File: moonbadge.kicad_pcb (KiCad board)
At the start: 2 copper layers, 49.5 x 147.2 mm, 61 parts, among them J1 Conn_01x04, J10 105162-0001, J2 USB_B_Micro, J3 Conn_01x02, J4 Conn_01x02, J5 Conn_01x02, J6 Conn_01x04, J7 Conn_01x02, J8 Conn_01x02, J9 Conn_01x02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

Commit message: split boards into top and bottom
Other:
- outline, holes or cut-outs redrawn

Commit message: removed designators, more cosmetic fixes
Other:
- board text added: "MoonBadge.github.io"
- board text added: "Moonbadge Rev.1 Alex Camilo"

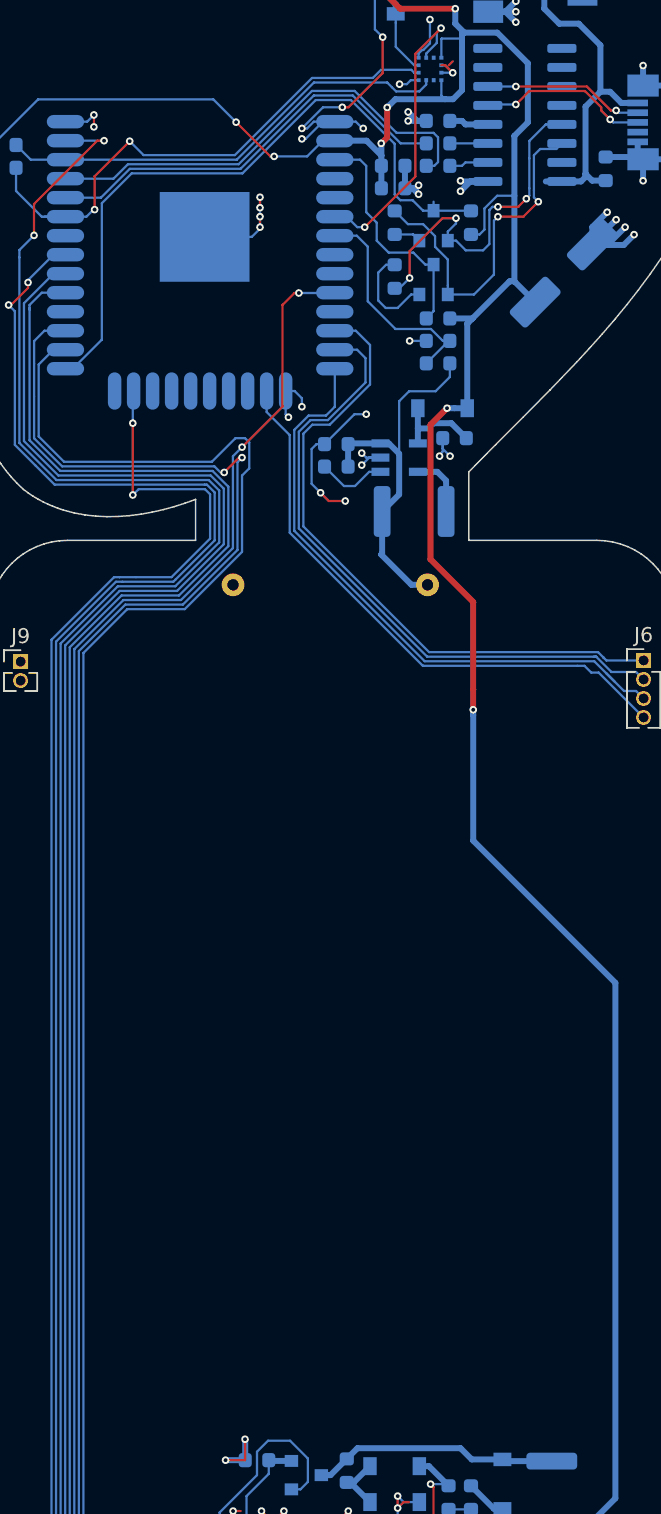
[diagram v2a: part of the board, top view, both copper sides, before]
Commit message: Rev 2
Swapped TX/RX
Swapped battery polarity
nudged battery down by 1mm to clear boost coil
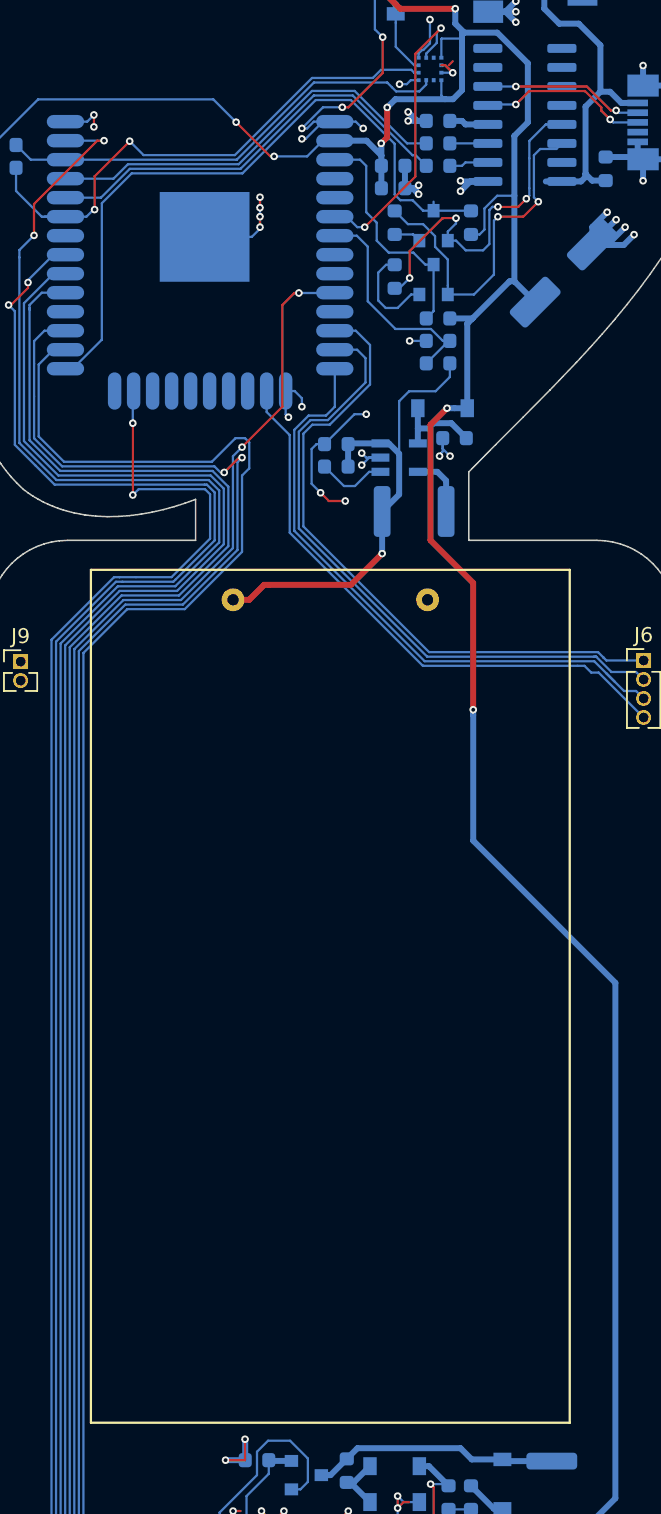
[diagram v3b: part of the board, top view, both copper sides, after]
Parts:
- BT1: moved to F.Cu
- moved BT1 1.00 mm to (139.9, 81.7)
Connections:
- R11 pad 1: RxD -> TxD
- R8 pad 1: TxD -> RxD
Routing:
- net BAT: track 24.9 -> 32.2 mm, vias 0 -> 1
- net TxD: track 31.2 -> 28.0 mm
- net RxD: track 28.3 -> 28.9 mm
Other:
- board text added: "Moonbadge Rev.2 Alex Camilo"
- board text removed: "Moonbadge Rev.1 Alex Camilo"
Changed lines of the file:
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@@
   (page A4)
   (layers
-    (0 F.Cu signal)
+    (0 F.Cu signal hide)
     (31 B.Cu signal)
     (32 B.Adhes user)
@@
     (35 F.Paste user)
     (36 B.SilkS user)
-    (37 F.SilkS user hide)
+    (37 F.SilkS user)
     (38 B.Mask user)
     (39 F.Mask user)
@@
     (visible_elements 7FFFFFFF)
     (pcbplotparams
-      (layerselection 0x010fc_ffffffff)
+      (layerselection 0x010f0_7ffffffe)
       (usegerberextensions false)
       (usegerberattributes false)
@@
       (padsonsilk false)
       (subtractmaskfromsilk false)
-      (outputformat 1)
+      (outputformat 5)
       (mirror false)
-      (drillshape 1)
+      (drillshape 0)
       (scaleselection 1)
-      (outputdirectory ""))
+      (outputdirectory "holes"))
   )
   (net 0 "")
@@
     )
   )
-  (module 12BH321P-GR:12BH321P-GR (layer B.Cu)
-    (at 139.9 80.7 90)
-    (fp_text reference BT1 (at -40 17 -90) (layer B.SilkS) hide
-      (effects (font (size 1 1) (thickness 0.15)) (justify mirror))
+  (module 12BH321P-GR:12BH321P-GR (layer F.Cu)
+    (at 139.9 81.7 90)
+    (fp_text reference BT1 (at -40 -17 90) (layer F.SilkS) hide
+      (effects (font (size 1 1) (thickness 0.15)))
     )
-    (fp_text value Battery_Cell (at -49 17 -90) (layer B.Fab)
-      (effects (font (size 1 1) (thickness 0.15)) (justify mirror))
+    (fp_text value Battery_Cell (at -49 -17 90) (layer F.Fab)
+      (effects (font (size 1 1) (thickness 0.15)))
     )
-    (fp_line (start -55 16) (end -55 -16) (layer B.SilkS) (width 0.15))
-    (fp_line (start 2 -16) (end -55 -16) (layer B.SilkS) (width 0.15))
-    (fp_line (start 2 0) (end 2 -16) (layer B.SilkS) (width 0.15))
-    (fp_line (start 2 16) (end 2 0) (layer B.SilkS) (width 0.15))
-    (fp_line (start 2 16) (end -55 16) (layer B.SilkS) (width 0.15))
-    (pad 1 thru_hole circle (at 0 6.5 90) (size 1.524 1.524) (drill 0.762) (layers *.Cu *.Mask)
+    (fp_line (start -55 -16) (end -55 16) (layer F.SilkS) (width 0.15))
+    (fp_line (start 2 16) (end -55 16) (layer F.SilkS) (width 0.15))
+    (fp_line (start 2 0) (end 2 16) (layer F.SilkS) (width 0.15))
+    (fp_line (start 2 -16) (end 2 0) (layer F.SilkS) (width 0.15))
+    (fp_line (start 2 -16) (end -55 -16) (layer F.SilkS) (width 0.15))
+    (pad 1 thru_hole circle (at 0 -6.5 90) (size 1.524 1.524) (drill 0.762) (layers *.Cu *.Mask)
       (net 2 BAT))
-    (pad 2 thru_hole circle (at 0 -6.5 90) (size 1.524 1.524) (drill 0.762) (layers *.Cu *.Mask)
+    (pad 2 thru_hole circle (at 0 6.5 90) (size 1.524 1.524) (drill 0.762) (layers *.Cu *.Mask)
       (net 4 GND))
   )
@@
     )
     (pad 1 smd roundrect (at -0.7875 0) (size 0.875 0.95) (layers B.Cu B.Paste B.Mask) (roundrect_rratio 0.25)
-      (net 7 TxD))
+      (net 6 RxD))
     (pad 2 smd roundrect (at 0.7875 0) (size 0.875 0.95) (layers B.Cu B.Paste B.Mask) (roundrect_rratio 0.25)
       (net 66 "Net-(R8-Pad2)"))
@@
       (net 67 "Net-(R11-Pad2)"))
     (pad 1 smd roundrect (at -0.7875 0) (size 0.875 0.95) (layers B.Cu B.Paste B.Mask) (roundrect_rratio 0.25)
-      (net 6 RxD))
+      (net 7 TxD))
     (model ${KISYS3DMOD}/Capacitor_SMD.3dshapes/C_0603_1608Metric.wrl
       (at (xyz 0 0 0))
@@
     (effects (font (size 1.5 1.5) (thickness 0.3)))
   )
-  (gr_text "Moonbadge Rev.1\nAlex Camilo" (at 120.5 99.7 90) (layer B.SilkS)
+  (gr_text "Moonbadge Rev.2\nAlex Camilo" (at 120.5 99.7 90) (layer B.SilkS)
     (effects (font (size 1.5 1.5) (thickness 0.3)) (justify mirror))
   )
@@
   (segment (start 143.3 51.2) (end 143.7 50.8) (width 0.4) (layer F.Cu) (net 1))
   (segment (start 143.7 50.8) (end 143.7 48.8) (width 0.4) (layer F.Cu) (net 1))
-  (segment (start 146.593599 70.006401) (end 146.593599 78.993599) (width 0.4) (layer F.Cu) (net 1))
   (segment (start 147.7 68.9) (end 146.593599 70.006401) (width 0.4) (layer F.Cu) (net 1))
-  (segment (start 146.593599 78.993599) (end 149.45 81.85) (width 0.4) (layer F.Cu) (net 1))
-  (segment (start 149.45 81.85) (end 149.45 87.7) (width 0.4) (layer F.Cu) (net 1))
-  (segment (start 149.45 87.7) (end 149.45 89.05) (width 0.4) (layer F.Cu) (net 1))
   (segment (start 144.562 42.2) (end 143.51 41.148) (width 0.4) (layer F.Cu) (net 1))
   (segment (start 148.25 42.2) (end 144.562 42.2) (width 0.4) (layer F.Cu) (net 1))
@@
   (segment (start 131.96 166.55) (end 133.05 166.55) (width 0.1524) (layer B.Cu) (net 1))
   (segment (start 133.05 166.55) (end 133.1 166.5) (width 0.1524) (layer B.Cu) (net 1))
+  (segment (start 149.45 80.5779) (end 146.593599 77.721499) (width 0.4) (layer F.Cu) (net 1))
+  (segment (start 149.45 89.05) (end 149.45 80.5779) (width 0.4) (layer F.Cu) (net 1))
+  (segment (start 146.593599 70.006401) (end 146.593599 77.721499) (width 0.4) (layer F.Cu) (net 1))
   (segment (start 141.0875 71.3) (end 141.0875 72.8) (width 0.4) (layer B.Cu) (net 2))
   (segment (start 143.3625 78.61513) (end 143.3625 75.8) (width 0.4) (layer B.Cu) (net 2))
-  (segment (start 146.4 80.7) (end 145.32237 80.7) (width 0.4) (layer B.Cu) (net 2))
-  (segment (start 145.32237 80.7) (end 143.3 78.67763) (width 0.4) (layer B.Cu) (net 2))
   (segment (start 143.3 78.67763) (end 143.3625 78.61513) (width 0.4) (layer B.Cu) (net 2))
   (segment (start 143.809322 71.25) (end 144.5 71.940678) (width 0.4) (layer B.Cu) (net 2))
@@
   (segment (start 146.934467 67.765533) (end 147.8875 66.8125) (width 0.1524) (layer B.Cu) (net 2))
   (segment (start 147.8875 66.8125) (end 147.8875 65.9) (width 0.1524) (layer B.Cu) (net 2))
+  (via (at 143.3625 78.61513) (size 0.508) (drill 0.254) (layers F.Cu B.Cu) (net 2))
+  (segment (start 141.27763 80.7) (end 143.3625 78.61513) (width 0.4) (layer F.Cu) (net 2))
+  (segment (start 135.47763 80.7) (end 135.818 80.7) (width 0.4) (layer F.Cu) (net 2))
+  (segment (start 134.47763 81.7) (end 135.47763 80.7) (width 0.4) (layer F.Cu) (net 2))
+  (segment (start 133.4 81.7) (end 134.47763 81.7) (width 0.4) (layer F.Cu) (net 2))
+  (segment (start 135.818 80.7) (end 141.27763 80.7) (width 0.4) (layer F.Cu) (net 2))
   (segment (start 140.2 52.29) (end 141.885164 52.29) (width 0.1524) (layer B.Cu) (net 3))
   (segment (start 143 57.7) (end 143.8 58.5) (width 0.1524) (layer B.Cu) (net 3))
@@
   (segment (start 146.8 55.7) (end 149.2875 55.7) (width 0.1524) (layer B.Cu) (net 5))
   (segment (start 149.2875 55.7) (end 149.3 55.7125) (width 0.1524) (layer B.Cu) (net 5))
-  (segment (start 146.3125 51.2) (end 144.6 51.2) (width 0.1524) (layer B.Cu) (net 6))
-  (segment (start 138.8 48) (end 133.9 52.9) (width 0.1524) (layer B.Cu) (net 6))
-  (segment (start 141.4 48) (end 138.8 48) (width 0.1524) (layer B.Cu) (net 6))
   (segment (start 124.57 54.83) (end 122.2 54.83) (width 0.1524) (layer B.Cu) (net 6))
-  (segment (start 144.6 51.2) (end 141.4 48) (width 0.1524) (layer B.Cu) (net 6))
   (segment (start 126.5 52.9) (end 124.57 54.83) (width 0.1524) (layer B.Cu) (net 6))
+  (segment (start 146.3125 52.7) (end 145.60889 51.99639) (width 0.1524) (layer B.Cu) (net 6))
+  (segment (start 145.60889 51.99639) (end 145.39639 51.99639) (width 0.1524) (layer B.Cu) (net 6))
+  (segment (start 145.39639 51.99639) (end 141.4 48) (width 0.1524) (layer B.Cu) (net 6))
+  (segment (start 141.4 48) (end 138.8 48) (width 0.1524) (layer B.Cu) (net 6))
+  (segment (start 138.8 48) (end 133.9 52.9) (width 0.1524) (layer B.Cu) (net 6))
   (segment (start 133.9 52.9) (end 126.5 52.9) (width 0.1524) (layer B.Cu) (net 6))
-  (segment (start 144.327456 50.49639) (end 141.526257 47.695191) (width 0.1524) (layer B.Cu) (net 7))
+  (segment (start 125.408934 53.56) (end 122.2 53.56) (width 0.1524) (layer B.Cu) (net 7))
+  (segment (start 145.031066 51.2) (end 141.526257 47.695191) (width 0.1524) (layer B.Cu) (net 7))
+  (segment (start 146.3125 51.2) (end 145.031066 51.2) (width 0.1524) (layer B.Cu) (net 7))
   (segment (start 138.673744 47.69519) (end 133.773744 52.59519) (width 0.1524) (layer B.Cu) (net 7))
-  (segment (start 147.1 52.45) (end 147.1 50.8) (width 0.1524) (layer B.Cu) (net 7))
   (segment (start 141.526257 47.695191) (end 138.673744 47.69519) (width 0.1524) (layer B.Cu) (net 7))
-  (segment (start 146.3125 52.7) (end 146.85 52.7) (width 0.1524) (layer B.Cu) (net 7))
-  (segment (start 146.85 52.7) (end 147.1 52.45) (width 0.1524) (layer B.Cu) (net 7))
-  (segment (start 125.408934 53.56) (end 122.2 53.56) (width 0.1524) (layer B.Cu) (net 7))
   (segment (start 133.773744 52.59519) (end 126.373744 52.59519) (width 0.1524) (layer B.Cu) (net 7))
   (segment (start 126.373744 52.59519) (end 125.408934 53.56) (width 0.1524) (layer B.Cu) (net 7))
-  (segment (start 146.79639 50.49639) (end 144.327456 50.49639) (width 0.1524) (layer B.Cu) (net 7))
-  (segment (start 147.1 50.8) (end 146.79639 50.49639) (width 0.1524) (layer B.Cu) (net 7))
   (segment (start 120.1 55.25) (end 120.1 57.35) (width 0.1524) (layer F.Cu) (net 8))
   (segment (start 124.78 51.02) (end 124.33 51.02) (width 0.1524) (layer F.Cu) (net 8))

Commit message: Added tek logo, removed files.
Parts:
- removed J1: Conn_01x04, Connector_PinHeader_1.27mm:PinHeader_1x04_P1.27mm_Vertical
- removed J3, J4, J5: Conn_01x02, Connector_PinHeader_1.27mm:PinHeader_1x02_P1.27mm_Vertical
- removed the svg2mod at (200.8, 100.3)
- added svg2mod: G***, tek-logo:tek-logo, B.Cu at (152.8, 167.8)
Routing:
- net T7: track 152.4 -> 43.9 mm, vias 1 -> 0
- net T6: track 138.7 -> 43.6 mm, vias 1 -> 0
- net T4: track 113.5 -> 38.9 mm, vias 1 -> 0
- net T5: track 108.0 -> 41.4 mm, vias 1 -> 0
- net +3V3: track 249.6 -> 248.3 mm
- removed copper zone on F.Cu, net (none)
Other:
- outline, holes or cut-outs redrawn
